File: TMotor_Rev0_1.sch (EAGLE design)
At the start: 37 parts, among them U1 INA125U, U2 INA125U

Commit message: Created quad board CAN board with both the Teensy and Nano.
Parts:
- removed J3: (no value), SparkFun-Connectors:CONN_07
- removed TRQ-LA, TRQ-RA: (no value), SparkFun-Connectors:CONN_03X2SHROUD
- added B_PFET, G_PFET, R_PFET, S_P_FET: 2SJ305TE85LF, 2SJ305TE85LF:2SJ305TE85LF
- added C1, C2: 1uF, rcl:C-EU050-024X044
- added C10, C11, C17, C18, C21, C22, C23: 100nF, rcl:C-EU050-024X044
- added J10, J7, J8, J9: 5015680207, SnapEDA-Library:5015680207
- added JL, JL1, JR, JR1: 5015680407, SnapEDA-Library:5015680407
- added R10, R9: 22k, resistor:R-US_0207/10
- added R11, R12: 120R, rcl:R-US_0207/10
- added R13, R15: 470R, rcl:R-US_0207/10
- added R3: 47R, rcl:R-US_0207/10
- added R4, R5: 100R, rcl:R-US_0207/10
- added R6: 150R, rcl:R-US_0207/10
- added RESET, STOP, SYNC_DEFAULT, SYNC_LED: (no value), SparkFun-Connectors:CONN_02
- added RGB_LED: (no value), con-lstb:MA04-1
- added U$1: TEENSY_3.5/3.6_EXTERNAL_W/RESET, Teensy356:TEENSY_3.5/3.6_EXTERNAL_W/RESET
- added U$2, U$3, U$4, U$5: XT30PW-F, XT30PW-M:XT30PW-F
- added U3, U4: INA125U, Digikey:INA125U
- added U5: SN65HVD230MDREP, SnapEDA-Library:SN65HVD230MDREP
- C3, C5, C9: value 0.1uF -> 100nF
- J1, J2: value (none) -> 5015680507; device SparkFun-Connectors:CONN_10" -> SnapEDA-Library:5015680507
- R14: value 3.3k -> 470R
- R16: value 1k -> 470R
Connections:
- net SCL1 renamed SCL0
- net SDA1 renamed SDA0
- removed net A0: C12.1, U1.SENSE, U1.VO, USB.A0
- removed net A1: USB.A1
- removed net A2: C19.2, R8.2, TRQ-LA.5, USB.A2
- removed net A3: C20.1, R7.2, TRQ-RA.5, USB.A3
- removed net A6: C6.1, U2.SENSE, U2.VO, USB.A6
- removed net A7: USB.A7
- removed net CAN_CS: J1.2, USB.D10
- removed net CAN_INT: J1.6, USB.D8
- removed net D4: USB.D4
- removed net D5: USB.D5
- removed net D6: USB.D6
- removed net D7: USB.D7
- removed net H_CS: J2.9, J3.3
- removed net H_INT: J2.5, J3.7
- removed net H_MISO: J2.8, J3.4
- removed net H_MOSI: J2.7, J3.5
- removed net H_SCK: J2.6, J3.6
- removed net LLS_OE: J1.10, USB.D9
- removed net PWM-LL: USB.D3
- new net BLUE_LED_SIG: B_PFET.GATE, U$1.26
- new net CANRX: U$1.4, U5.R
- new net CANTX: U$1.3, U5.D
- new net FSR_HEEL_L: C1.2, J2.5, R10.2, U$1.33/A14
- new net FSR_HEEL_R: C2.1, J1.5, R9.2, U$1.21/A7
- new net FSR_TOE_L: C19.2, J2.4, R8.2, U$1.34/A15
- new net FSR_TOE_R: C20.1, J1.4, R7.2, U$1.20/A6
- new net GREEN_LED_SIG: G_PFET.GATE, U$1.27
- new net N$1: R4.2, RGB_LED.1
- new net N$14: U4.VREF5
- new net N$15: U4.IAREF, U4.VREFBG, U4.VREFOUT
- new net N$16: R13.1, U4.RG_2
- new net N$17: R3.2, S_P_FET.DRAIN
- new net N$18: R3.1, SYNC_LED.2
- new net N$19: U4.VREF2.5
- new net N$2: B_PFET.DRAIN, R4.1
- new net N$24: R6.2, RGB_LED.4
- new net N$25: R5.2, RGB_LED.2
- new net N$30: G_PFET.DRAIN, R5.1
- new net N$31: R6.1, R_PFET.DRAIN
- new net N$32: U3.IAREF, U3.VREFBG, U3.VREFOUT
- new net N$33: C22.1, JL1.2, U3.V+IN
- new net N$34: C21.1, JL1.4, U3.V-IN
- new net N$35: R15.2, U3.RG
- new net N$36: R15.1, U3.RG_2
- new net N$4: U4.VREF10
- new net N$40: U3.VREF10
- new net N$41: U3.VREF5
- new net N$42: U3.VREF2.5
- new net N$44: J10.1, J7.1, J8.1, J9.1, R11.2, R12.2, U5.CANH
- new net N$45: J10.2, J7.2, J8.2, J9.2, R11.1, R12.1, U5.CANL
- new net NANO_CS: U$1.10/CS, USB.D10
- new net NRESET: POGO.5, SWD.NRESET
- new net RED_LED_SIG: R_PFET.GATE, U$1.28
- new net RESET: RESET.1, U$1.RESET, USB.RST_1
- new net STOP: STOP.1, U$1.6
- new net SW3.3V: POGO.2, SWD.VCC
- new net SWCLK: POGO.4, SWD.SWDCLK
- new net SWDIO: POGO.1, SWD.SWDIO
- new net SWGND: POGO.6, SWD.GND@1, SWD.GND@2
- new net SYNC_DEFAULT: SYNC_DEFAULT.1, U$1.25
- new net SYNC_SIG: S_P_FET.GATE, U$1.29/PWM
- new net TRQ_AMP_L: C12.1, U$1.36/A17, U1.SENSE, U1.VO
- new net TRQ_AMP_L1: C18.1, U$1.35/A16, U3.SENSE, U3.VO
- new net TRQ_AMP_R: C6.1, U$1.23/A9, U2.SENSE, U2.VO
- new net TRQ_AMP_R1: C10.1, U$1.22/A8, U4.SENSE, U4.VO
- net 3.3V: now also J1.2, J2.1, J2.2, JL.1, JL1.1, JR.1, JR1.1, U$1.3V3, U3.!SLEEP, U3.V+, U4.!SLEEP, U4.V+, U5.VCC; no longer TRQ-LA.3, TRQ-LA.6, TRQ-RA.3, TRQ-RA.6, USB.3.3V
- net GND: now also C1.1, C10.2, C11.2, C17.2, C18.2, C2.2, C21.2, C22.2, C23.1, JL.3, JL1.3, JR.3, JR1.3, R10.1, R9.1, RESET.2, RGB_LED.3, STOP.2, SYNC_DEFAULT.2, SYNC_LED.1, U$1.AGND, U$1.GND, U$1.GND2, U$2.-, U$3.-, U$4.-, U$5.-, U3.V-, U3.VREFCOM, U4.V-, U4.VREFCOM, U5.GND, U5.RS; no longer J2.1, J3.2, TRQ-LA.1, TRQ-RA.1
- net MISO: now also U$1.12/MISO; no longer J1.3
- net MOSI: now also U$1.11/MOSI; no longer J1.4
- net N$10: now also JL.2; no longer TRQ-LA.2
- net N$11: now also JL.4; no longer TRQ-LA.4
- net N$27: now also R13.2, U4.RG; no longer J1.7
- net N$28: now also C17.1, JR1.2, U4.V+IN; no longer J1.8
- net N$29: now also C11.1, JR1.4, U4.V-IN; no longer J1.9
- net N$8: now also JR.2; no longer TRQ-RA.2
- net N$9: now also JR.4; no longer TRQ-RA.4
- net SCK: now also U$1.13/SCK; no longer J1.5
- net VCC: now also U$2.+, U$3.+, U$4.+, U$5.+
- net VIN: now also B_PFET.SOURCE, C23.2, G_PFET.SOURCE, R_PFET.SOURCE, S_P_FET.SOURCE, U$1.VIN; no longer J2.10, J3.1

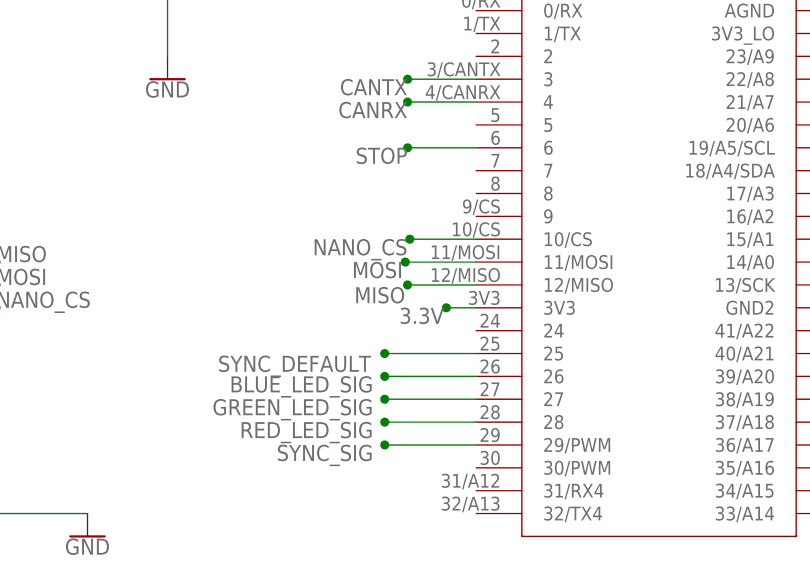
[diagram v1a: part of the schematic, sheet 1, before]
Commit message: cross connected the spi coms pins due to TSPISlave function
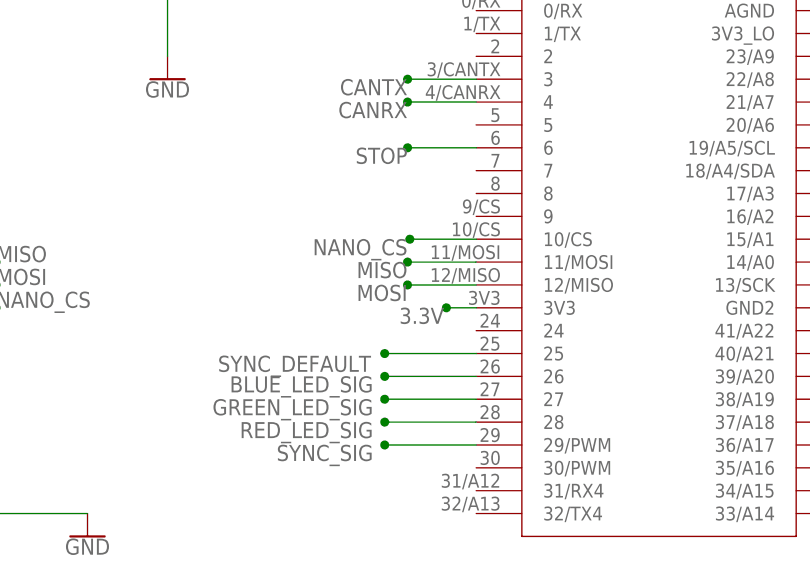
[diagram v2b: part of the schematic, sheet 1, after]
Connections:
- net MISO: now also U$1.11/MOSI; no longer U$1.12/MISO
- net MOSI: now also U$1.12/MISO; no longer U$1.11/MOSI
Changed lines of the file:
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@@
 </segment>
 <segment>
-<wire x1="152.4" y1="40.64" x2="144.526" y2="40.64" width="0.1524" layer="91"/>
-<junction x="144.526" y="40.64"/>
-<label x="144.272" y="40.64" size="1.778" layer="95" rot="R180"/>
-<pinref part="U$1" gate="G$1" pin="11/MOSI"/>
+<pinref part="U$1" gate="G$1" pin="12/MISO"/>
+<wire x1="152.4" y1="38.1" x2="144.78" y2="38.1" width="0.1524" layer="91"/>
+<junction x="144.78" y="38.1"/>
+<label x="144.78" y="38.1" size="1.778" layer="95" rot="R180"/>
 </segment>
 </net>
@@
 </segment>
 <segment>
-<wire x1="152.4" y1="38.1" x2="144.78" y2="38.1" width="0.1524" layer="91"/>
-<junction x="144.78" y="38.1"/>
-<label x="144.526" y="37.846" size="1.778" layer="95" rot="R180"/>
-<pinref part="U$1" gate="G$1" pin="12/MISO"/>
+<pinref part="U$1" gate="G$1" pin="11/MOSI"/>
+<wire x1="152.4" y1="40.64" x2="144.78" y2="40.64" width="0.1524" layer="91"/>
+<junction x="144.78" y="40.64"/>
+<label x="144.78" y="40.64" size="1.778" layer="95" rot="R180"/>
 </segment>
 </net>
